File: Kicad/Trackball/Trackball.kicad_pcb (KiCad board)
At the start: 2 copper layers, 429.8 x 138.1 mm, 91 parts, among them J1 Battery, J10 Conn_01x04_Female, J11 Conn_01x04_Male, J12 Conn_01x04_Female, J13 Conn_01x04_Female, J14 Conn_01x04_Female, J15 Conn_01x04_Female, J16 Conn_01x04_Male, J17 Conn_01x04_Male, J18 Conn_01x03_Pin, J19 Conn_01x03_Pin, J2 Conn_01x04_Male, J20 Conn_01x03_Socket, J21 Conn_01x03_Socket, J22 Conn_01x04_Male, J23 Conn_01x04_Male, J24 Conn_01x04_Male, J25 Conn_01x04_Male, J3 Conn_01x04_Male, J4 Conn_01x04_Male, J5 Conn_01x04_Male, J6 Conn_01x04_Male, J7 Conn_01x04_Male, J8 Conn_01x04_Male, J9 Conn_01x04_Male, SW1 SW_SPDT, SW2 SW_SPDT, SW3 SW_SPDT, U1 ProMicro, U3 TCR2EF19, U4 PMW3610

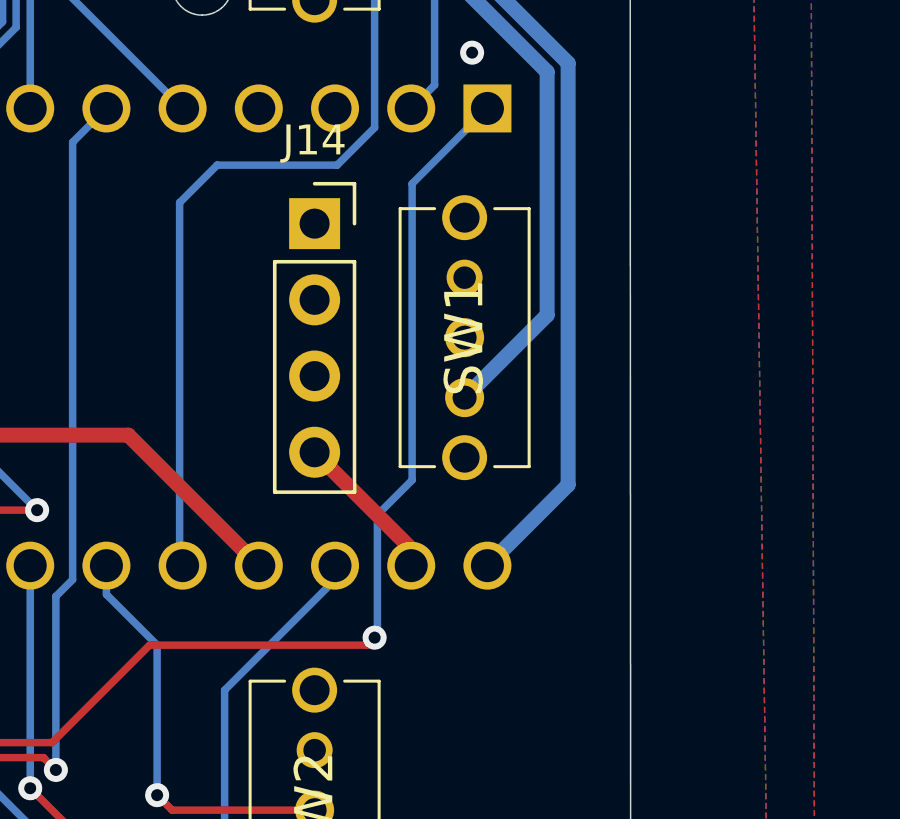
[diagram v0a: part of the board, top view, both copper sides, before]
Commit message: B4: Regenerated Gerbers for the middle and bottom decks, sent for manufacturing.
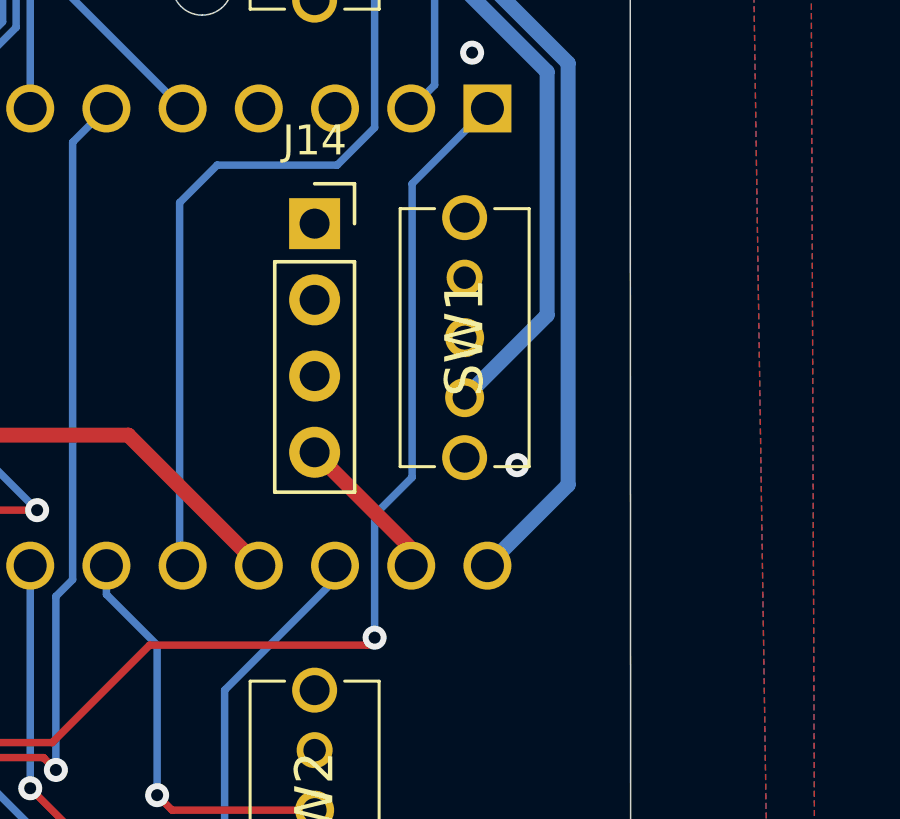
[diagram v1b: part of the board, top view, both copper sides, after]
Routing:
- net GND: vias 42 -> 43
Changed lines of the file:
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@@
+	)
+	(via
+		(at 183.65 105.85)
+		(size 0.8)
+		(drill 0.4)
+		(layers "F.Cu" "B.Cu")
+		(free yes)
+		(net 1)
 	)
 	(via
@@
 	)
 	(segment
+		(start 178.994 111.506)
+		(end 178.9 111.6)
+		(width 0.25)
+		(layer "B.Cu")
+		(net 5)
+	)
+	(segment
+		(start 178.9 107.506)
+		(end 178.9 111.506)
+		(width 0.25)
+		(layer "B.Cu")
+		(net 5)
+	)
+	(segment
 		(start 180.15 96.47)
-		(end 180.15 106.35)
-		(width 0.25)
-		(layer "B.Cu")
-		(net 5)
-	)
-	(segment
-		(start 178.994 107.506)
-		(end 178.994 111.506)
+		(end 180.15 106.256)
 		(width 0.25)
 		(layer "B.Cu")
@@
 	)
 	(segment
-		(start 180.15 106.35)
-		(end 178.994 107.506)
-		(width 0.25)
-		(layer "B.Cu")
-		(net 5)
-	)
-	(segment
-		(start 178.994 111.506)
-		(end 178.9 111.6)
-		(width 0.25)
-		(layer "B.Cu")
+		(start 180.15 106.256)
+		(end 178.9 107.506)
+		(width 0.25)
+		(layer "B.Cu")

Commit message: B4: Corrected orientation switch labels, moved the battery tie-down holes to its center. TODO: recreate Gerbers.
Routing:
- net Button2: track 47.7 -> 50.9 mm
- net BTReset: track 62.6 -> 64.5 mm
- net +3V3: track 43.1 -> 44.8 mm
- net GND: vias 43 -> 41
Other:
- outline, holes or cut-outs redrawn
- board text added: "ORIENTATION BACK-FRONT"
- board text added: "ORIENTATION FRONT-BACK"
- board text removed: "CONTROL FINGER-THUMB"
- board text removed: "CONTROL THUMB-FINGER"

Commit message: B4: Moved the ball size label to a place readable in assembled unit.
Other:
- board text added: "44mm Ball"
- board text added: "52.5mm Ball"
- board text added: "55mm Ball"
- board text added: "u/ak66666 ThumbsUp! Trackball v4"
- board text removed: "u/ak66666 ThumbsUp! Trackball v4 44mm Ball"
- board text removed: "u/ak66666 ThumbsUp! Trackball v4 52.5mm Ball"
- board text removed: "u/ak66666 ThumbsUp! Trackball v4 55mm Ball"
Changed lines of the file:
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@@
 		)
 	)
-	(gr_text "u/ak66666\nThumbsUp! Trackball v4\n52.5mm Ball"
+	(gr_text "u/ak66666\nThumbsUp! Trackball v4"
 		(at 259.4 101.6 90)
 		(layer "B.SilkS")
@@
 		)
 	)
-	(gr_text "u/ak66666\nThumbsUp! Trackball v4\n44mm Ball"
+	(gr_text "u/ak66666\nThumbsUp! Trackball v4"
 		(at 344.4 102.6 90)
 		(layer "B.SilkS")
@@
 		)
 	)
+	(gr_text "55mm Ball"
+		(at 374.1 101.54 90)
+		(layer "B.SilkS")
+		(effects
+			(font
+				(size 1.5 1.5)
+				(thickness 0.3)
+				(bold yes)
+			)
+			(justify bottom mirror)
+		)
+	)
 	(gr_text "GND"
 		(at 145.5 122.45 0)
@@
 		)
 	)
-	(gr_text "u/ak66666\nThumbsUp! Trackball v4\n55mm Ball"
+	(gr_text "u/ak66666\nThumbsUp! Trackball v4"
 		(at 432.4 102.6 90)
 		(layer "B.SilkS")
@@
 			)
 			(justify left bottom mirror)
+		)
+	)
+	(gr_text "52.5mm Ball"
+		(at 201.42 101.86 90)
+		(layer "B.SilkS")
+		(effects
+			(font
+				(size 1.5 1.5)
+				(thickness 0.3)
+				(bold yes)
+			)
+			(justify bottom mirror)
 		)
 	)
@@
 		)
 	)
+	(gr_text "44mm Ball"
+		(at 287.56 101.55 90)
+		(layer "B.SilkS")
+		(effects
+			(font
+				(size 1.5 1.5)
+				(thickness 0.3)
+				(bold yes)
+			)
+			(justify bottom mirror)
+		)
+	)
